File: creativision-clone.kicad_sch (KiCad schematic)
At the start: 92 parts, among them J1 Conn_01x10_Socket, J2 Conn_01x10_Socket, J3 Conn_01x07_Pin, J4 Conn_01x04_Socket, J5 RCJ-013, J6 RCJ-014, P1 Cartridge Slot, Q1 2n4401, SW1 Reset, U1 AS6C62256-DIP, U100 74HCT574, U101 74HCT574, U102 74HCT574, U12 74LS32, U15 74LS139, U18 AS6C62256-DIP, U2 6502, U20 27256, U21 6821, U22 SN76489AN, U3 TMS9918A, U99 74HCT04, X1 2MHz

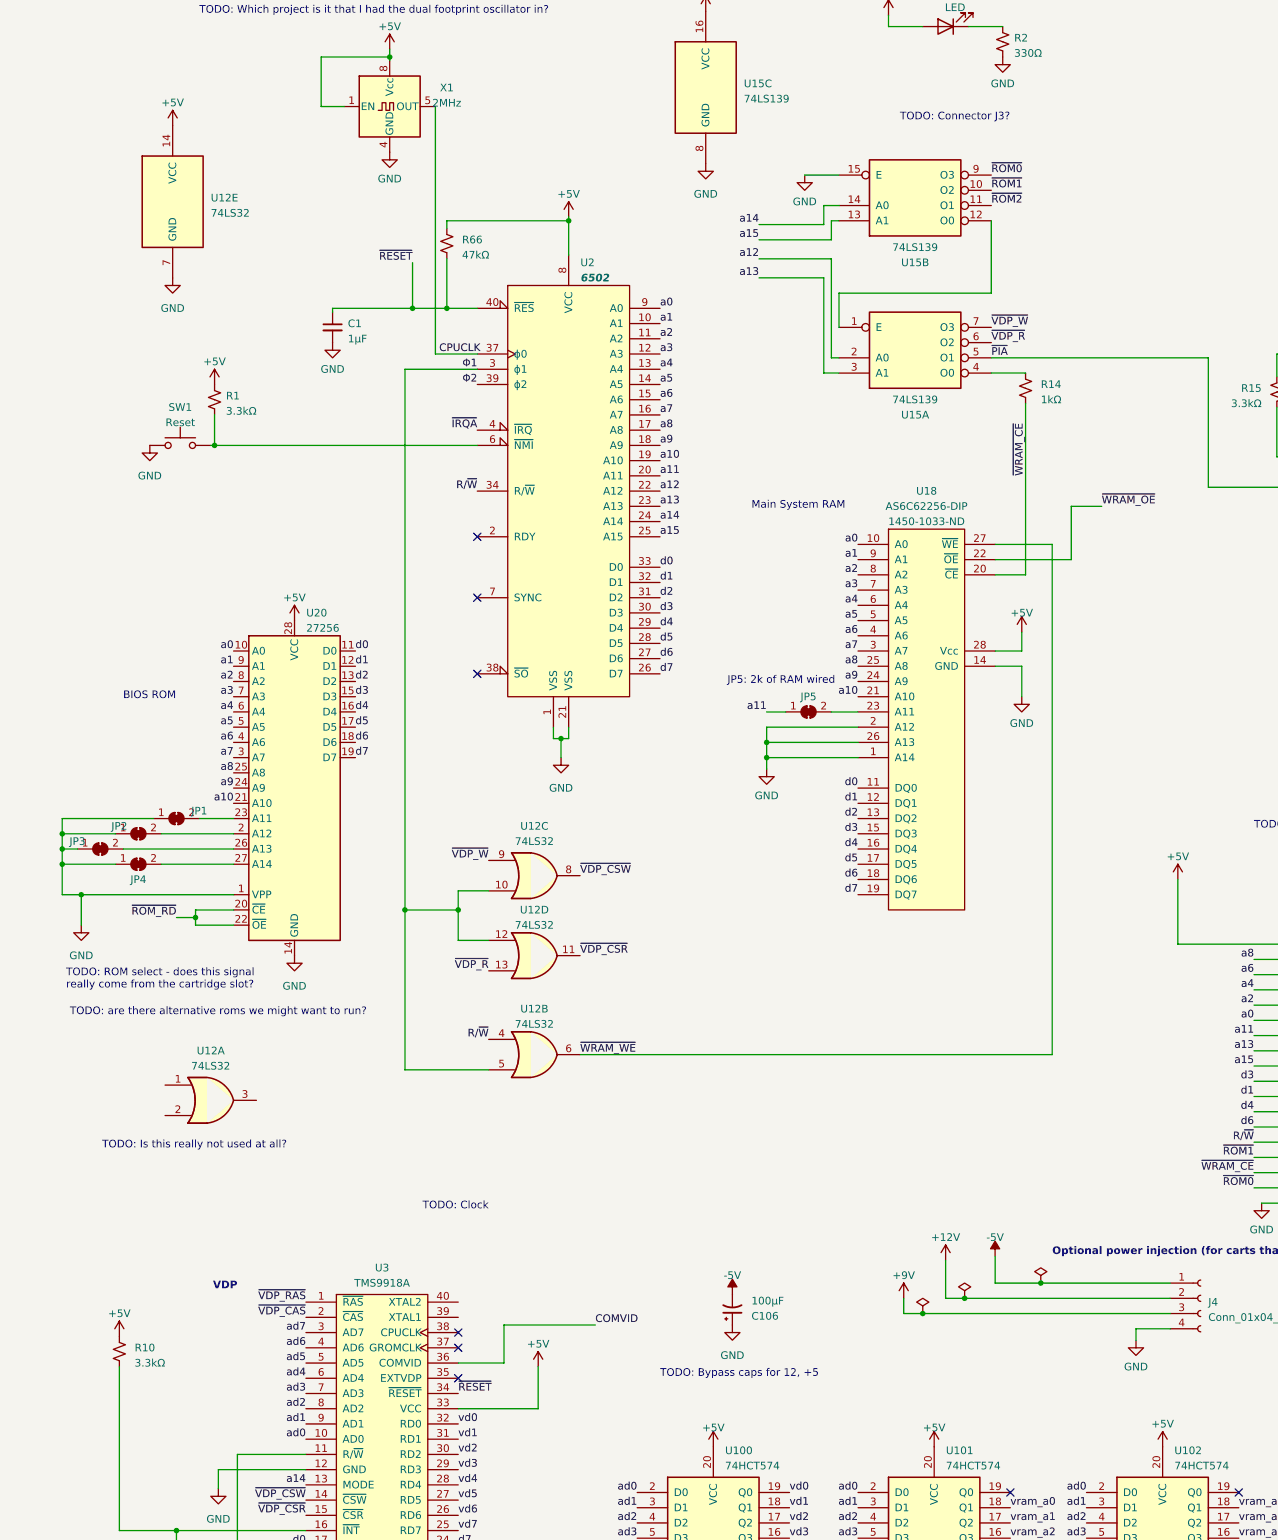
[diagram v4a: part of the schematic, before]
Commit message: TMS9918 Xtal, bypass caps for optional Vs
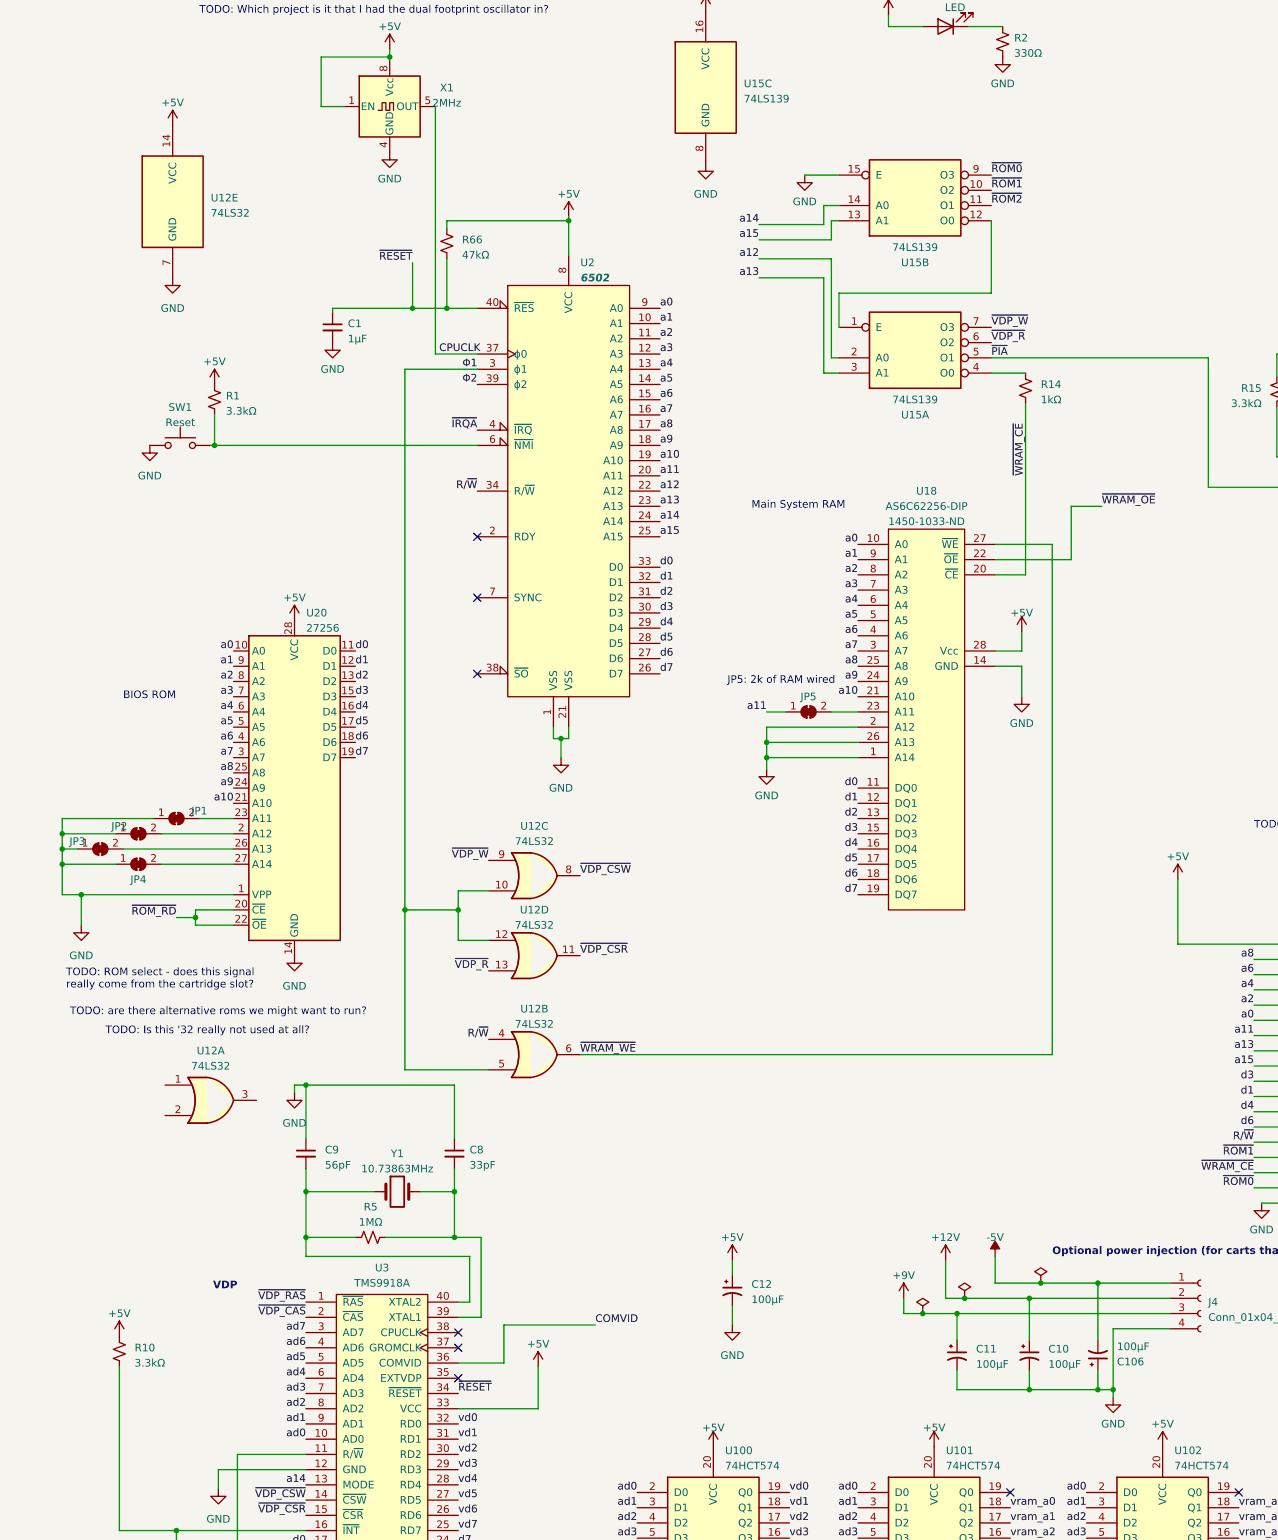
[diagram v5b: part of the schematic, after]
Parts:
- added C10, C11, C12: 100µF, symbol Device:C_Polarized_Small_US
- added C8: 33pF, symbol Device:C_Small
- added C9: 56pF, symbol Device:C_Small
- added R5: 1MΩ, symbol Device:R_Small_US
- added Y1: 10.73863MHz, Crystal:Crystal_HC49-4H_Vertical, symbol Device:Crystal
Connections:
- net +12V: now also C10.1
- net +5V: now also C12.1
- net +9V: now also C11.1
- net GND: now also C10.2, C11.2, C12.2, C8.1, C9.1
- net at U3.39 (XTAL1): now also C8.2, R5.1, Y1.2
- net at U3.40 (XTAL2): now also C9.2, R5.2, Y1.1
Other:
- note added: "TODO: Is this '32 really not used at all?"
- note removed: "TODO: Bypass caps for 12, +5"
- note removed: "TODO: Clock"
- note removed: "TODO: Connector J3?"
- note removed: "TODO: Is this really not used at all?"
- moved on the sheet: C106

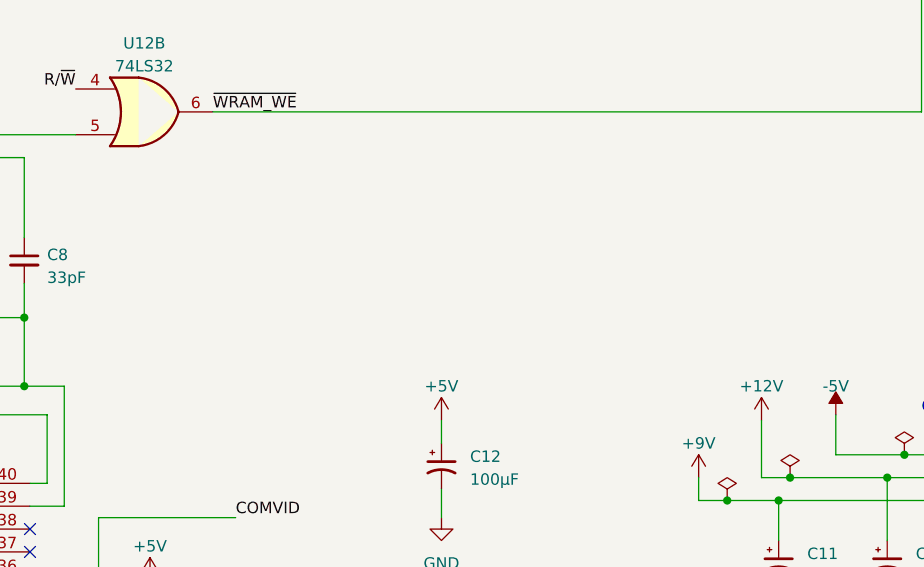
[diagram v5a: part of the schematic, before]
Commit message: Power switch
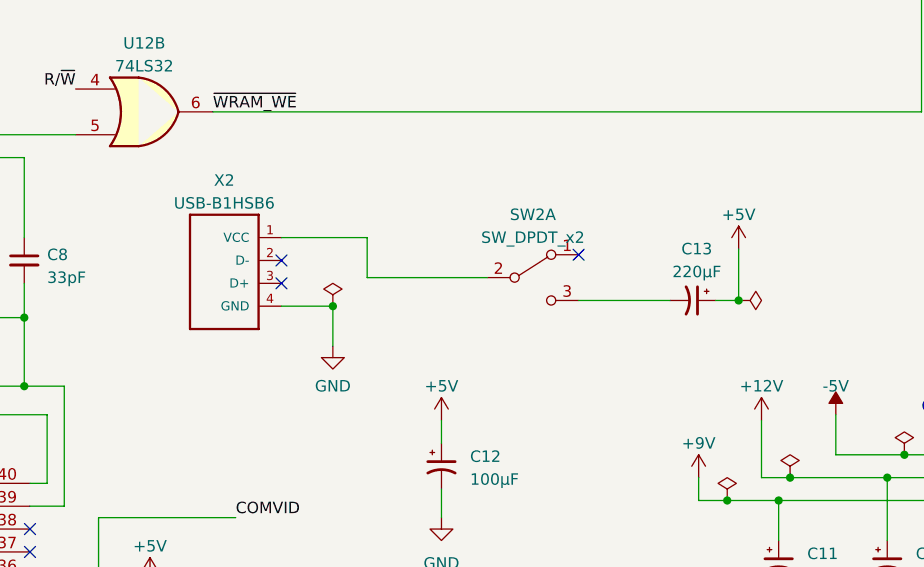
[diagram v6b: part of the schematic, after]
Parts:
- added C13: 220µF, symbol Device:C_Polarized_Small_US
- added SW2: SW_DPDT_x2, symbol Switch:SW_DPDT_x2
- added X2: USB-B1HSB6, OST_USB-B1HSB6, symbol USB-B1HSB6-2:USB-B1HSB6
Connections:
- net +5V: now also C13.1
- net GND: now also X2.4 (GND)
- new net: C13.2, SW2.3 (C)
- new net: SW2.2 (B), X2.1 (VCC)
- no-connect marks 8 -> 11
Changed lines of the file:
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@@
   (junction (at 310.515 73.025) (diameter 0) (color 0 0 0 0)
   )
+  (junction (at 113.03 214.63) (diameter 0) (color 0 0 0 0)
+  )
   (junction (at 325.755 165.735) (diameter 0) (color 0 0 0 0)
   )
@@
   (junction (at 302.895 76.835) (diameter 0) (color 0 0 0 0)
   )
+  (junction (at 158.115 213.995) (diameter 0) (color 0 0 0 0)
+  )
   (junction (at 313.055 75.565) (diameter 0) (color 0 0 0 0)
   )
@@
   )
   (no_connect (at 79.375 239.395))
+  (no_connect (at 107.315 212.09))
   (no_connect (at 82.55 116.84))
   (no_connect (at 82.55 129.54))
@@
   (no_connect (at 209.55 266.065))
   (no_connect (at 171.45 266.065))
+  (no_connect (at 140.335 208.915))
   (no_connect (at 79.375 241.935))
+  (no_connect (at 107.315 209.55))
   (no_connect (at 79.375 247.015))
   (wire (pts (xy 371.475 79.375) (xy 371.475 83.82))
@@
     (stroke (width 0) (type default))
   )
+  (wire (pts (xy 107.315 207.01) (xy 116.84 207.01))
+    (stroke (width 0) (type default))
+  )
   (wire (pts (xy 348.615 38.735) (xy 347.345 38.735))
     (stroke (width 0) (type default))
@@
     (stroke (width 0) (type default))
   )
+  (wire (pts (xy 113.03 219.075) (xy 113.03 214.63))
+    (stroke (width 0) (type default))
+  )
   (wire (pts (xy 174.625 233.68) (xy 174.625 240.665))
     (stroke (width 0) (type default))
@@
     (stroke (width 0) (type default))
   )
+  (wire (pts (xy 113.03 214.63) (xy 107.315 214.63))
+    (stroke (width 0) (type default))
+  )
   (wire (pts (xy 329.565 80.645) (xy 329.565 74.295))
     (stroke (width 0) (type default))
@@
     (stroke (width 0) (type default))
   )
+  (wire (pts (xy 155.575 213.995) (xy 158.115 213.995))
+    (stroke (width 0) (type default))
+  )
   (wire (pts (xy 331.47 69.215) (xy 332.74 69.215))
     (stroke (width 0) (type default))
@@
     (stroke (width 0) (type default))
   )
+  (wire (pts (xy 158.115 208.28) (xy 158.115 213.995))
+    (stroke (width 0) (type default))
+  )
   (wire (pts (xy 130.81 143.51) (xy 130.81 140.97))
     (stroke (width 0) (type default))
@@
     (stroke (width 0) (type default))
   )
+  (wire (pts (xy 140.335 213.995) (xy 150.495 213.995))
+    (stroke (width 0) (type default))
+  )
   (wire (pts (xy 271.78 45.085) (xy 269.24 45.085))
     (stroke (width 0) (type default))
@@
     (stroke (width 0) (type default))
   )
+  (wire (pts (xy 116.84 211.455) (xy 130.175 211.455))
+    (stroke (width 0) (type default))
+  )
   (wire (pts (xy 276.86 233.045) (xy 276.86 229.235))
     (stroke (width 0) (type default))
@@
     (stroke (width 0) (type default))
   )
+  (wire (pts (xy 116.84 207.01) (xy 116.84 211.455))
+    (stroke (width 0) (type default))
+  )
   (wire (pts (xy 300.99 40.005) (xy 269.24 40.005))
     (stroke (width 0) (type default))
@@
     )
   )
+  (symbol (lib_id "power:PWR_FLAG") (at 113.03 214.63 0) (unit 1)
+    (in_bom yes) (on_board yes) (dnp no) (fields_autoplaced)
+    (property "Reference" "#FLG05" (at 113.03 212.725 0)
+      (effects (font (size 1.27 1.27)) hide)
+    )
+    (property "Value" "PWR_FLAG" (at 113.03 210.82 0)
+      (effects (font (size 1.27 1.27)) hide)
+    )
+    (property "Footprint" "" (at 113.03 214.63 0)
+      (effects (font (size 1.27 1.27)) hide)
+    )
+    (property "Datasheet" "~" (at 113.03 214.63 0)
+      (effects (font (size 1.27 1.27)) hide)
+    )
+    (pin "1")
+    (instances
+      (project "creativision-clone"
+        (path "/4f154aad-bddd-4366-bec7-a527fffe24b1"
+          (reference "#FLG05") (unit 1)
+        )
+      )
+    )
+  )
   (symbol (lib_id "power:+9V") (at 153.67 233.68 0) (unit 1)
     (in_bom yes) (on_board yes) (dnp no) (fields_autoplaced)
@@
     )
   )
+  (symbol (lib_id "Device:C_Polarized_Small_US") (at 153.035 213.995 270) (unit 1)
+    (in_bom yes) (on_board yes) (dnp no) (fields_autoplaced)
+    (property "Reference" "C13" (at 153.4668 208.28 90)
+      (effects (font (size 1.27 1.27)))
+    )
+    (property "Value" "220µF" (at 153.4668 210.82 90)
+      (effects (font (size 1.27 1.27)))
+    )
+    (property "Footprint" "" (at 153.035 213.995 0)
+      (effects (font (size 1.27 1.27)) hide)
+    )
+    (property "Datasheet" "~" (at 153.035 213.995 0)
+      (effects (font (size 1.27 1.27)) hide)
+    )
+    (pin "1")
+    (pin "2")
+    (instances
+      (project "creativision-clone"
+        (path "/4f154aad-bddd-4366-bec7-a527fffe24b1"
+          (reference "C13") (unit 1)
+        )
+      )
+    )
+  )
   (symbol (lib_id "power:GND") (at 52.07 176.53 0) (unit 1)
     (in_bom yes) (on_board yes) (dnp no) (fields_autoplaced)
@@
     )
   )
+  (symbol (lib_id "USB-B1HSB6-2:USB-B1HSB6") (at 104.775 209.55 0) (mirror y) (unit 1)
+    (in_bom yes) (on_board yes) (dnp no) (fields_autoplaced)
+    (property "Reference" "X2" (at 100.965 200.66 0)
+      (effects (font (size 1.27 1.27)))
+    )
+    (property "Value" "USB-B1HSB6" (at 100.965 203.2 0)
+      (effects (font (size 1.27 1.27)))
+    )
+    (property "Footprint" "OST_USB-B1HSB6" (at 104.775 209.55 0)
+      (effects (font (size 1.27 1.27)) (justify left bottom) hide)
+    )
+    (property "Datasheet" "" (at 104.775 209.55 0)
+      (effects (font (size 1.27 1.27)) (justify left bottom) hide)
+    )
+    (property "MANUFACTURER" "ON-SHORE TECHNOLOGY" (at 104.775 209.55 0)
+      (effects (font (size 1.27 1.27)) (justify left bottom) hide)
+    )
+    (property "DigiKey" "ED2983-ND\r" (at 104.775 209.55 0)
+      (effects (font (size 1.27 1.27)) hide)
+    )
+    (pin "1")
+    (pin "2")
+    (pin "3")
+    (pin "4")
+    (instances
+      (project "creativision-clone"
+        (path "/4f154aad-bddd-4366-bec7-a527fffe24b1"
+          (reference "X2") (unit 1)
+        )
+      )
+    )
+  )
   (symbol (lib_id "power:GND") (at 137.16 46.355 0) (unit 1)
     (in_bom yes) (on_board yes) (dnp no) (fields_autoplaced)
@@
     )
   )
+  (symbol (lib_id "Switch:SW_DPDT_x2") (at 135.255 211.455 0) (unit 1)
+    (in_bom yes) (on_board yes) (dnp no) (fields_autoplaced)
+    (property "Reference" "SW2" (at 135.255 204.47 0)
+      (effects (font (size 1.27 1.27)))
+    )
+    (property "Value" "SW_DPDT_x2" (at 135.255 207.01 0)
+      (effects (font (size 1.27 1.27)))
+    )
+    (property "Footprint" "" (at 135.255 211.455 0)
+      (effects (font (size 1.27 1.27)) hide)
+    )
+    (property "Datasheet" "~" (at 135.255 211.455 0)
+      (effects (font (size 1.27 1.27)) hide)
+    )
+    (pin "1")
+    (pin "2")
+    (pin "3")
+    (pin "4")
+    (pin "5")
+    (pin "6")
+    (instances
+      (project "creativision-clone"
+        (path "/4f154aad-bddd-4366-bec7-a527fffe24b1"
+          (reference "SW2") (unit 1)
+        )
+      )
+    )
+  )
   (symbol (lib_id "74xx:74LS32") (at 92.075 163.195 0) (unit 3)
     (in_bom yes) (on_board yes) (dnp no) (fields_autoplaced)
@@
     )
   )
+  (symbol (lib_id "power:PWR_FLAG") (at 158.115 213.995 270) (unit 1)
+    (in_bom yes) (on_board yes) (dnp no) (fields_autoplaced)
+    (property "Reference" "#FLG04" (at 160.02 213.995 0)
+      (effects (font (size 1.27 1.27)) hide)
+    )
+    (property "Value" "PWR_FLAG" (at 161.29 214.63 90)
+      (effects (font (size 1.27 1.27)) (justify left) hide)
+    )
+    (property "Footprint" "" (at 158.115 213.995 0)
+      (effects (font (size 1.27 1.27)) hide)
+    )
+    (property "Datasheet" "~" (at 158.115 213.995 0)
+      (effects (font (size 1.27 1.27)) hide)
+    )
+    (pin "1")
+    (instances
+      (project "creativision-clone"
+        (path "/4f154aad-bddd-4366-bec7-a527fffe24b1"
+          (reference "#FLG04") (unit 1)
+        )
+      )
+    )
+  )
   (symbol (lib_id "Device:C_Polarized_Small_US") (at 162.56 243.205 0) (unit 1)
     (in_bom yes) (on_board yes) (dnp no) (fields_autoplaced)
@@
     )
   )
+  (symbol (lib_id "power:+5V") (at 158.115 208.28 0) (unit 1)
+    (in_bom yes) (on_board yes) (dnp no) (fields_autoplaced)
+    (property "Reference" "#PWR068" (at 158.115 212.09 0)
+      (effects (font (size 1.27 1.27)) hide)
+    )
+    (property "Value" "+5V" (at 158.115 204.47 0)
+      (effects (font (size 1.27 1.27)))
+    )
+    (property "Footprint" "" (at 158.115 208.28 0)
+      (effects (font (size 1.27 1.27)) hide)
+    )
+    (property "Datasheet" "" (at 158.115 208.28 0)
+      (effects (font (size 1.27 1.27)) hide)
+    )
+    (pin "1")
+    (instances
+      (project "creativision-clone"
+        (path "/4f154aad-bddd-4366-bec7-a527fffe24b1"
+          (reference "#PWR068") (unit 1)
+        )
+      )
+    )
+  )
   (symbol (lib_id "Device:C_Small") (at 351.155 19.685 90) (unit 1)
     (in_bom yes) (on_board yes) (dnp no)
@@
         )
       )
+    )
+  )
+  (symbol (lib_id "power:GND") (at 113.03 219.075 0) (unit 1)
+    (in_bom yes) (on_board yes) (dnp no) (fields_autoplaced)
+    (property "Reference" "#PWR069" (at 113.03 225.425 0)
+      (effects (font (size 1.27 1.27)) hide)
+    )
+    (property "Value" "GND" (at 113.03 223.52 0)
+      (effects (font (size 1.27 1.27)))
+    )
+    (property "Footprint" "" (at 113.03 219.075 0)
+      (effects (font (size 1.27 1.27)) hide)
+    )
+    (property "Datasheet" "" (at 113.03 219.075 0)
+      (effects (font (size 1.27 1.27)) hide)
+    )
+    (pin "1")
+    (instances
+      (project "creativision-clone"
+        (path "/4f154aad-bddd-4366-bec7-a527fffe24b1"
+          (reference "#PWR069") (unit 1)
+        )
+      )
